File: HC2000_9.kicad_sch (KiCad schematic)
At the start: 14 parts

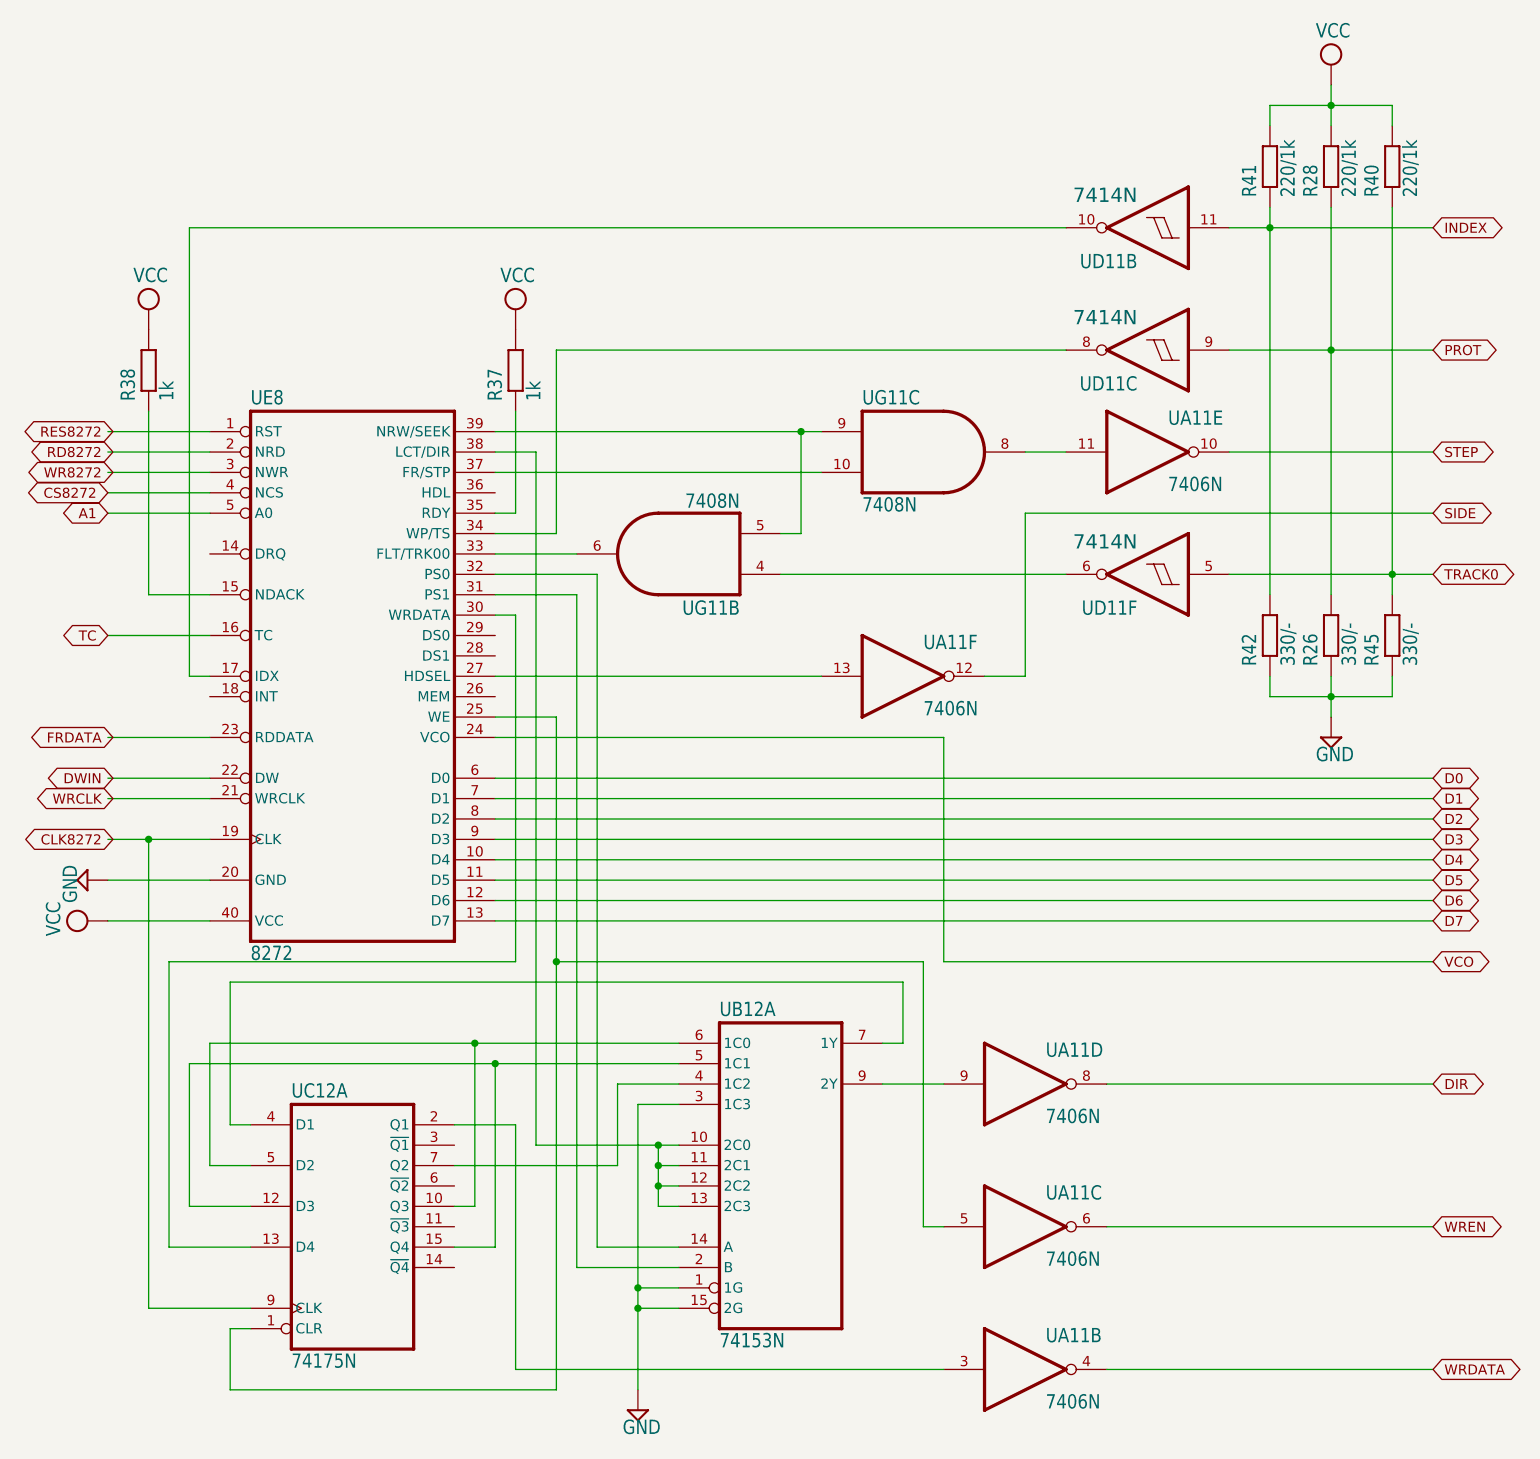
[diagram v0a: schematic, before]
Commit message: Fix errors (IC & unnoticed cut for 1 EPROM)
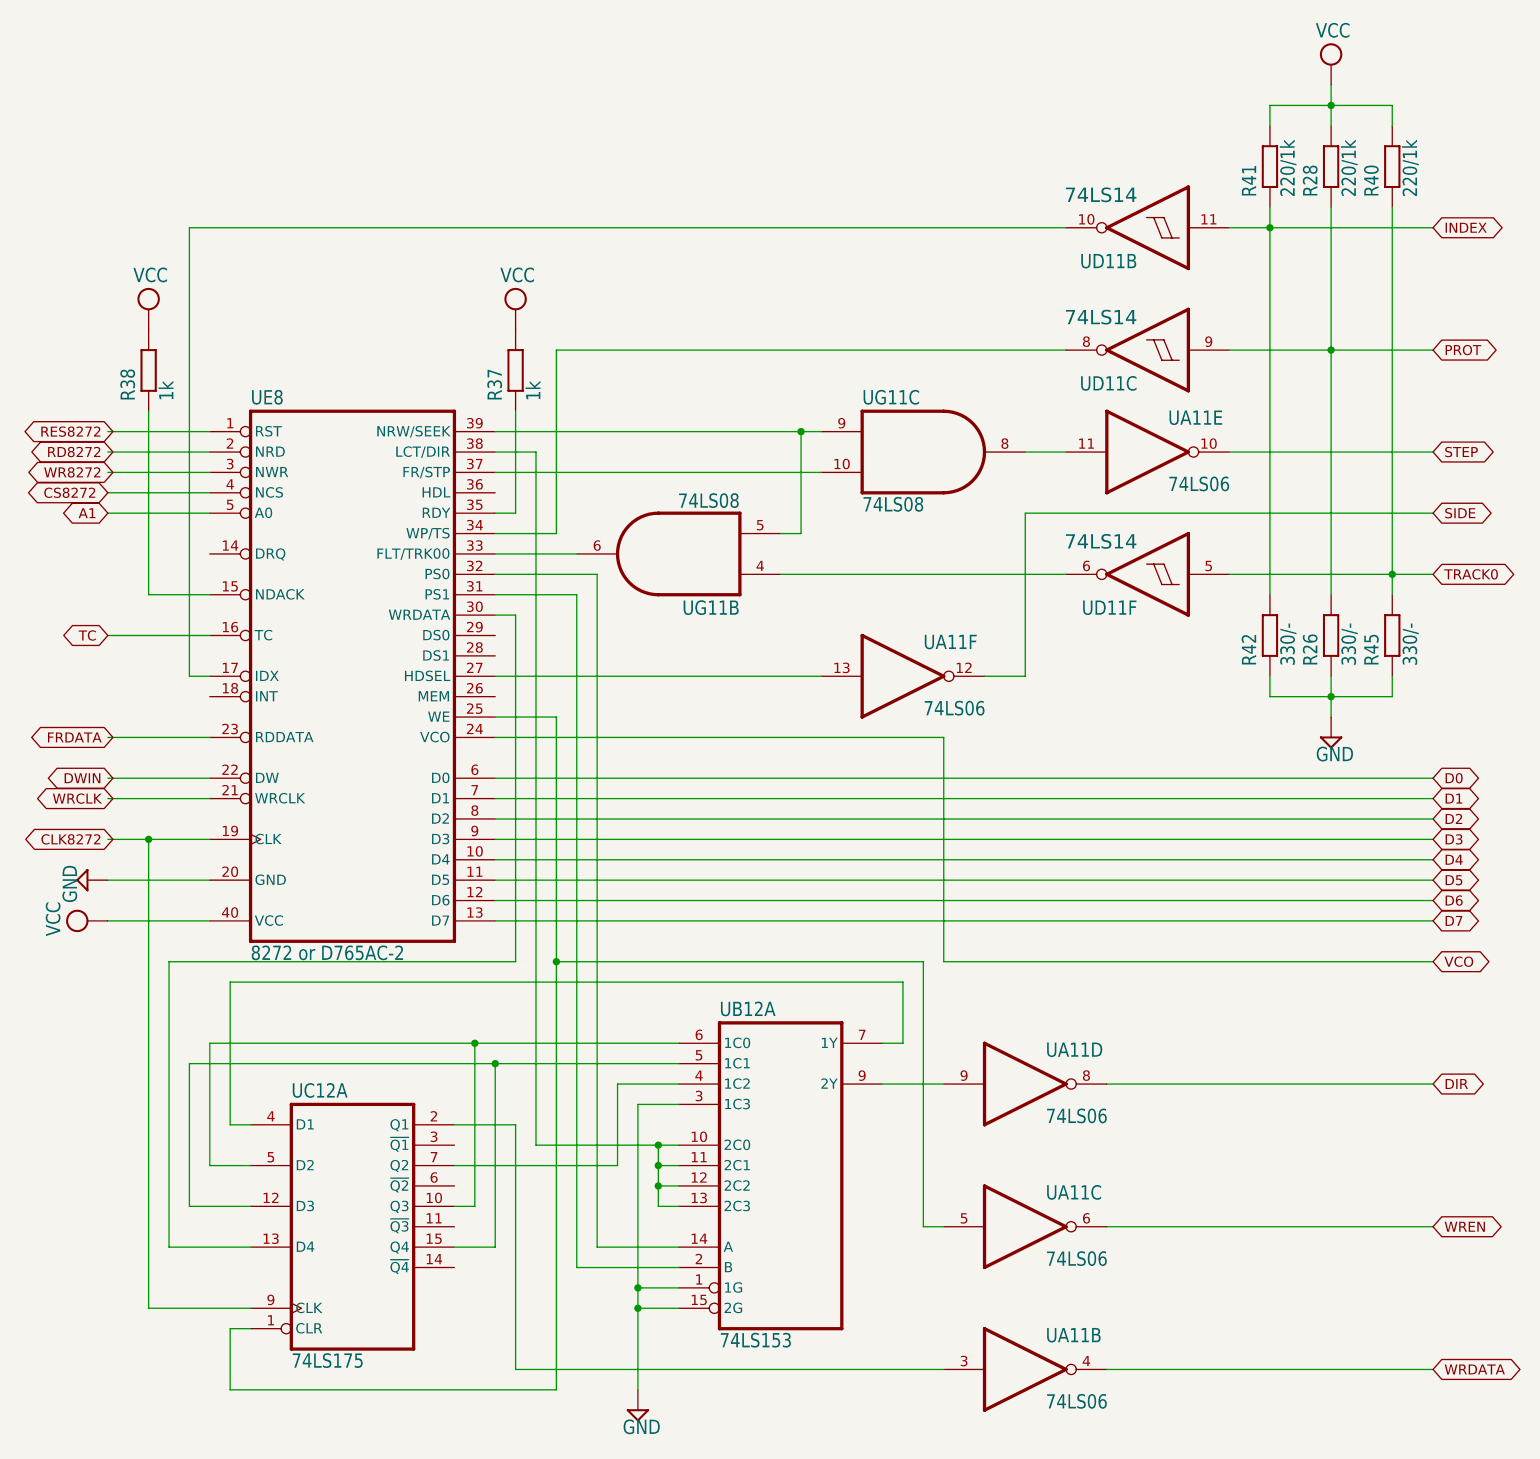
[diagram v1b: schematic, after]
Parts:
- UA11: value 7406N -> 74LS06
- UB12: value 74153N -> 74LS153
- UC12: value 74175N -> 74LS175
- UD11: value 7414N -> 74LS14
- UE8: value 8272 -> 8272 or D765AC-2
- UG11: value 7408N -> 74LS08
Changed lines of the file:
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@@
       (effects (font (size 1.778 1.5113)) (justify left bottom))
     )
-    (property "Value" "8272" (at 81.28 134.62 0)
+    (property "Value" "8272 or D765AC-2" (at 81.28 134.62 0)
       (effects (font (size 1.778 1.5113)) (justify left bottom))
     )
@@
       (effects (font (size 1.778 1.5113)) (justify left bottom))
     )
-    (property "Value" "7406N" (at 195.58 76.2 0)
+    (property "Value" "74LS06" (at 195.58 76.2 0)
       (effects (font (size 1.778 1.5113)) (justify left bottom))
     )
@@
       (effects (font (size 1.778 1.5113)) (justify left bottom))
     )
-    (property "Value" "7414N" (at 191.77 53.34 0)
+    (property "Value" "74LS14" (at 191.77 53.34 0)
       (effects (font (size 1.778 1.778)) (justify left bottom))
     )
@@
       (effects (font (size 1.778 1.5113)) (justify left bottom))
     )
-    (property "Value" "7408N" (at 157.48 78.74 0)
+    (property "Value" "74LS08" (at 157.48 78.74 0)
       (effects (font (size 1.778 1.5113)) (justify left bottom))
     )
@@
       (effects (font (size 1.778 1.5113)) (justify left bottom))
     )
-    (property "Value" "7406N" (at 180.34 154.94 0)
+    (property "Value" "74LS06" (at 180.34 154.94 0)
       (effects (font (size 1.778 1.5113)) (justify left bottom))
     )
@@
       (effects (font (size 1.778 1.5113)) (justify left bottom))
     )
-    (property "Value" "7406N" (at 165.1 104.14 0)
+    (property "Value" "74LS06" (at 165.1 104.14 0)
       (effects (font (size 1.778 1.5113)) (justify left bottom))
     )
@@
       (effects (font (size 1.778 1.5113)) (justify left bottom))
     )
-    (property "Value" "7414N" (at 191.77 81.28 0)
+    (property "Value" "74LS14" (at 191.77 81.28 0)
       (effects (font (size 1.778 1.778)) (justify left bottom))
     )
@@
       (effects (font (size 1.778 1.5113)) (justify left bottom))
     )
-    (property "Value" "74175N" (at 86.36 185.42 0)
+    (property "Value" "74LS175" (at 86.36 185.42 0)
       (effects (font (size 1.778 1.5113)) (justify left bottom))
     )
@@
       (effects (font (size 1.778 1.5113)) (justify left bottom))
     )
-    (property "Value" "7414N" (at 191.77 38.1 0)
+    (property "Value" "74LS14" (at 191.77 38.1 0)
       (effects (font (size 1.778 1.778)) (justify left bottom))
     )
@@
       (effects (font (size 1.778 1.5113)) (justify left bottom))
     )
-    (property "Value" "7406N" (at 180.34 190.5 0)
+    (property "Value" "74LS06" (at 180.34 190.5 0)
       (effects (font (size 1.778 1.5113)) (justify left bottom))
     )
@@
       (effects (font (size 1.778 1.5113)) (justify left bottom))
     )
-    (property "Value" "7408N" (at 142.24 76.2 0)
+    (property "Value" "74LS08" (at 142.24 76.2 0)
       (effects (font (size 1.778 1.5113)) (justify left bottom))
     )
@@
       (effects (font (size 1.778 1.5113)) (justify left bottom))
     )
-    (property "Value" "7406N" (at 180.34 172.72 0)
+    (property "Value" "74LS06" (at 180.34 172.72 0)
       (effects (font (size 1.778 1.5113)) (justify left bottom))
     )
@@
       (effects (font (size 1.778 1.5113)) (justify left bottom))
     )
-    (property "Value" "74153N" (at 139.7 182.88 0)
-      (effects (font (size 1.778 1.5113)) (justify left bottom))
-    )
+    (property "Value" "74LS153" (at 139.7 182.88 0)
+      (effects (font (size 1.778 1.5113)) (justify left bottom))
+    )

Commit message: Revision-E
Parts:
- R26, R42, R45: value 330/- -> -
- R28, R40, R41: value 220/1k -> 1k
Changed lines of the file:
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@@
       (effects (font (size 1.778 1.5113)) (justify left bottom))
     )
-    (property "Value" "220/1k" (at 219.202 39.37 0)
+    (property "Value" "1k" (at 219.202 39.37 0)
       (effects (font (size 1.778 1.5113)) (justify left bottom))
     )
@@
       (effects (font (size 1.778 1.5113)) (justify left bottom))
     )
-    (property "Value" "220/1k" (at 226.822 39.37 0)
+    (property "Value" "1k" (at 226.822 39.37 0)
       (effects (font (size 1.778 1.5113)) (justify left bottom))
     )
@@
       (effects (font (size 1.778 1.5113)) (justify left bottom))
     )
-    (property "Value" "330/-" (at 211.582 97.79 0)
+    (property "Value" "-" (at 211.582 97.79 0)
       (effects (font (size 1.778 1.5113)) (justify left bottom))
     )
@@
       (effects (font (size 1.778 1.5113)) (justify left bottom))
     )
-    (property "Value" "330/-" (at 219.202 97.79 0)
+    (property "Value" "-" (at 219.202 97.79 0)
       (effects (font (size 1.778 1.5113)) (justify left bottom))
     )
@@
       (effects (font (size 1.778 1.5113)) (justify left bottom))
     )
-    (property "Value" "330/-" (at 226.822 97.79 0)
+    (property "Value" "-" (at 226.822 97.79 0)
       (effects (font (size 1.778 1.5113)) (justify left bottom))
     )
@@
       (effects (font (size 1.778 1.5113)) (justify left bottom))
     )
-    (property "Value" "220/1k" (at 211.582 39.37 0)
-      (effects (font (size 1.778 1.5113)) (justify left bottom))
-    )
+    (property "Value" "1k" (at 211.582 39.37 0)
+      (effects (font (size 1.778 1.5113)) (justify left bottom))
+    )
